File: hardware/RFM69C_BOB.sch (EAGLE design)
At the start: 12 parts, among them U1 RFM69

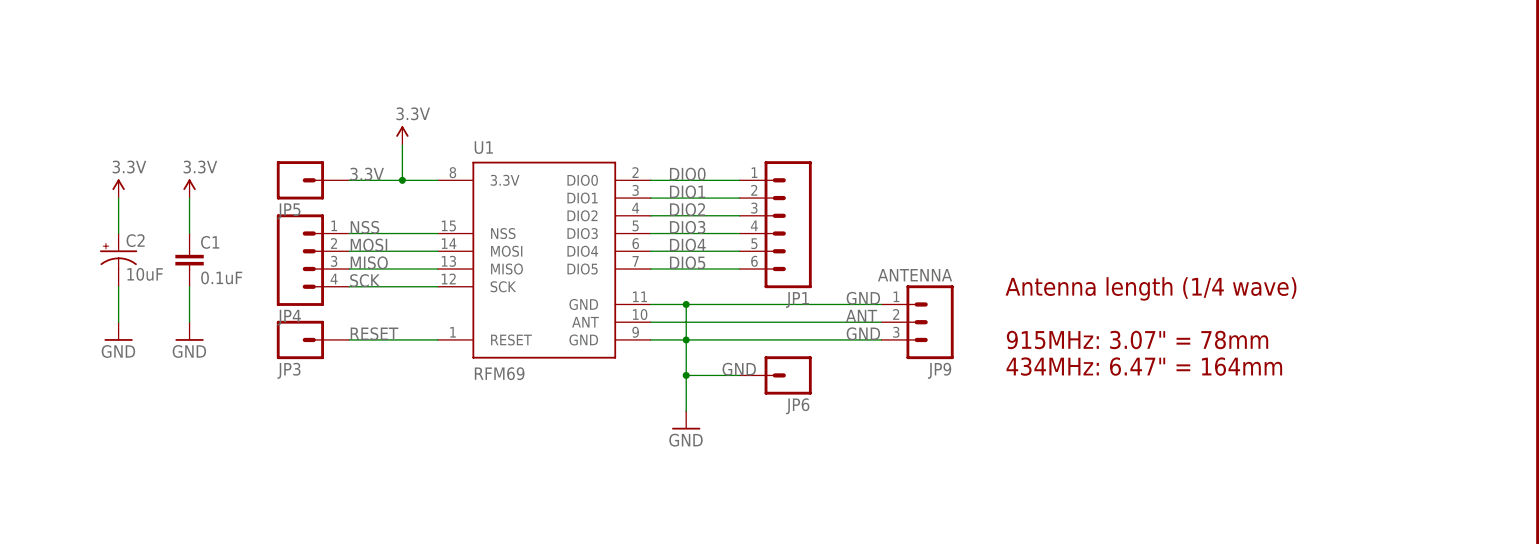
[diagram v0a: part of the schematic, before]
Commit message: Changed part to 'C' (compact) variant
New footprint, changed name to ensure proper variant is used (RFM69CW or
RFM69HCW)
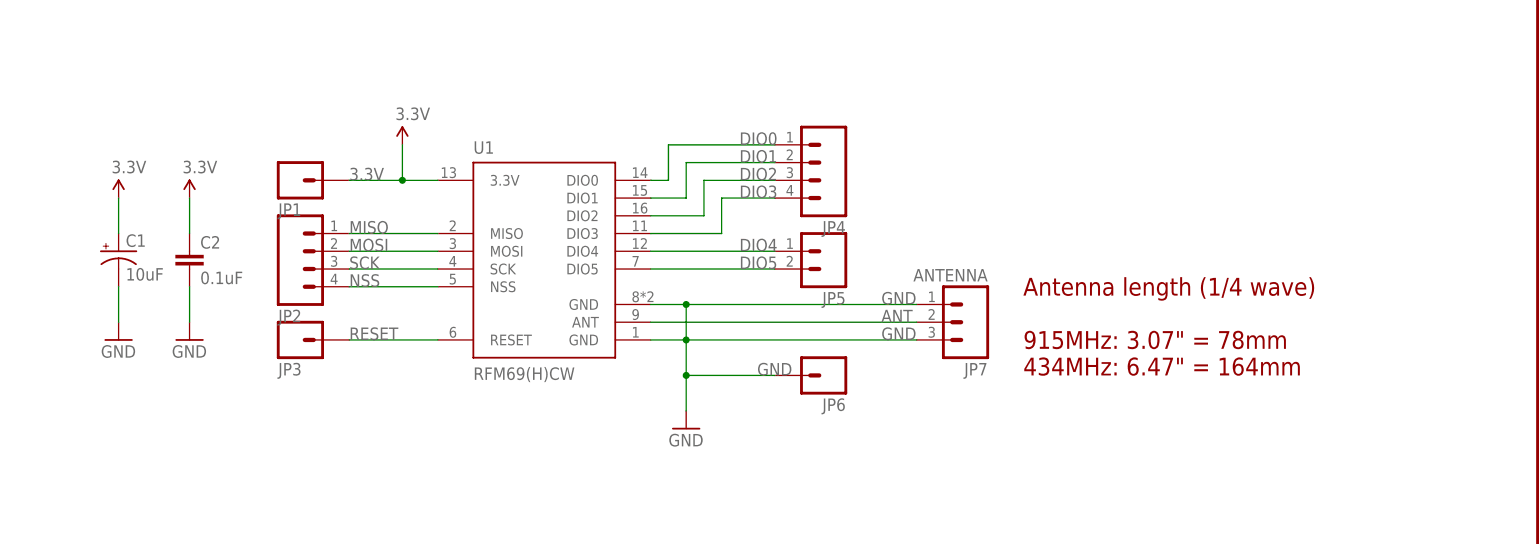
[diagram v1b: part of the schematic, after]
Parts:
- removed JP9: ANTENNA, mike-temp:M03_ROUND_ONLY_NO_SILK
- added JP2: (no value), mike-temp:M041X04_NO_SILK_ROUND
- added JP7: ANTENNA, mike-temp:M03_ROUND_ONLY_NO_SILK
- C1: value 0.1uF -> 10uF; device SparkFun-Capacitors:0.1UF-25V(+80/-20%)(0603) -> SparkFun-Capacitors:10UF-16V-10%(TANT)
- C2: value 10uF -> 0.1uF; device SparkFun-Capacitors:10UF-16V-10%(TANT) -> SparkFun-Capacitors:0.1UF-25V(+80/-20%)(0603)
- JP1: device mike-temp:M06_NOSILK_ROUND -> mike-temp:M01SMDNS
- JP5: device mike-temp:M01SMDNS -> mike-temp:M021X02_NO_SILK
- U1: value RFM69 -> RFM69(H)CW; device mike-temp:RFM69 -> mike-temp:RFM69CW
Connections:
- net 3.3V: now also C1.+, C2.1, JP1.1; no longer C1.1, C2.+, JP5.1
- net ANT: now also JP7.2; no longer JP9.2
- net DIO0: now also JP4.1; no longer JP1.1
- net DIO1: now also JP4.2; no longer JP1.2
- net DIO2: now also JP4.3; no longer JP1.3
- net DIO3: now also JP4.4; no longer JP1.4
- net DIO4: now also JP5.1; no longer JP1.5
- net DIO5: now also JP5.2; no longer JP1.6
- net GND: now also C1.-, C2.2, JP7.1, JP7.3; no longer C1.2, C2.-, JP9.1, JP9.3
- net MISO: now also JP2.1; no longer JP4.3
- net MOSI: now also JP2.2; no longer JP4.2
- net NSS: now also JP2.4; no longer JP4.1
- net SCK: now also JP2.3; no longer JP4.4
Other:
- moved on the sheet: JP4, JP6, U1
